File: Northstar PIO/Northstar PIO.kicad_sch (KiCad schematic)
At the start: 39 parts, among them J1 Conn_01x02, J1A1 Configuration Header, J2 Conn_01x02, J3 Conn_01x02, J4 Conn_01x02, J5 Conn_01x02, J6 Conn_01x02, J7 Conn_02x15_Odd_Even, P1 INPUT PORT, P2 OUTPUT PORT, U1B1 74LS74, U1C1 74LS74, U1D1 SN74LS164N, U2A1 74LS32, U2B1 74LS138, U2C1 74LS175, U2D1 74LS03, U2E1 74LS367, U3A1 74LS14, U3B1 74LS37, U3C1 74LS373, U3D1 74LS373

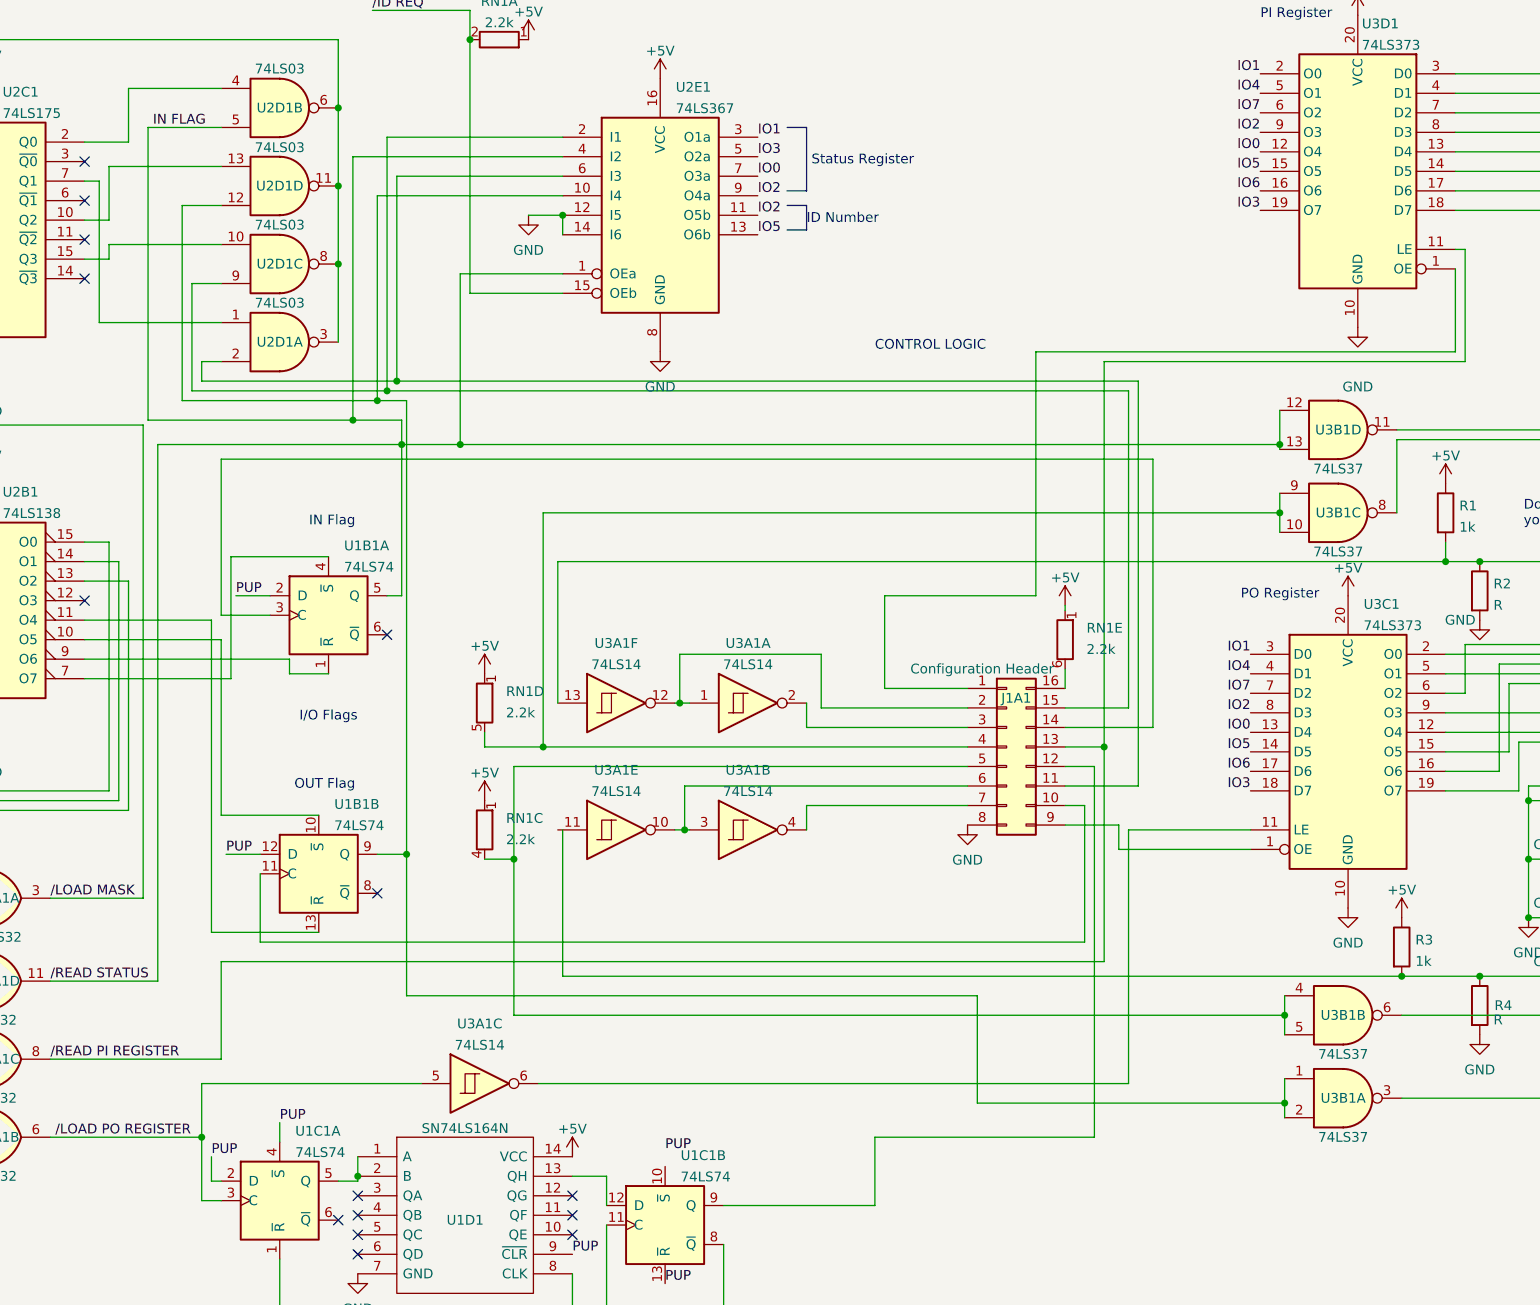
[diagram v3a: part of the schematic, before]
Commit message: fix pio problems discovered
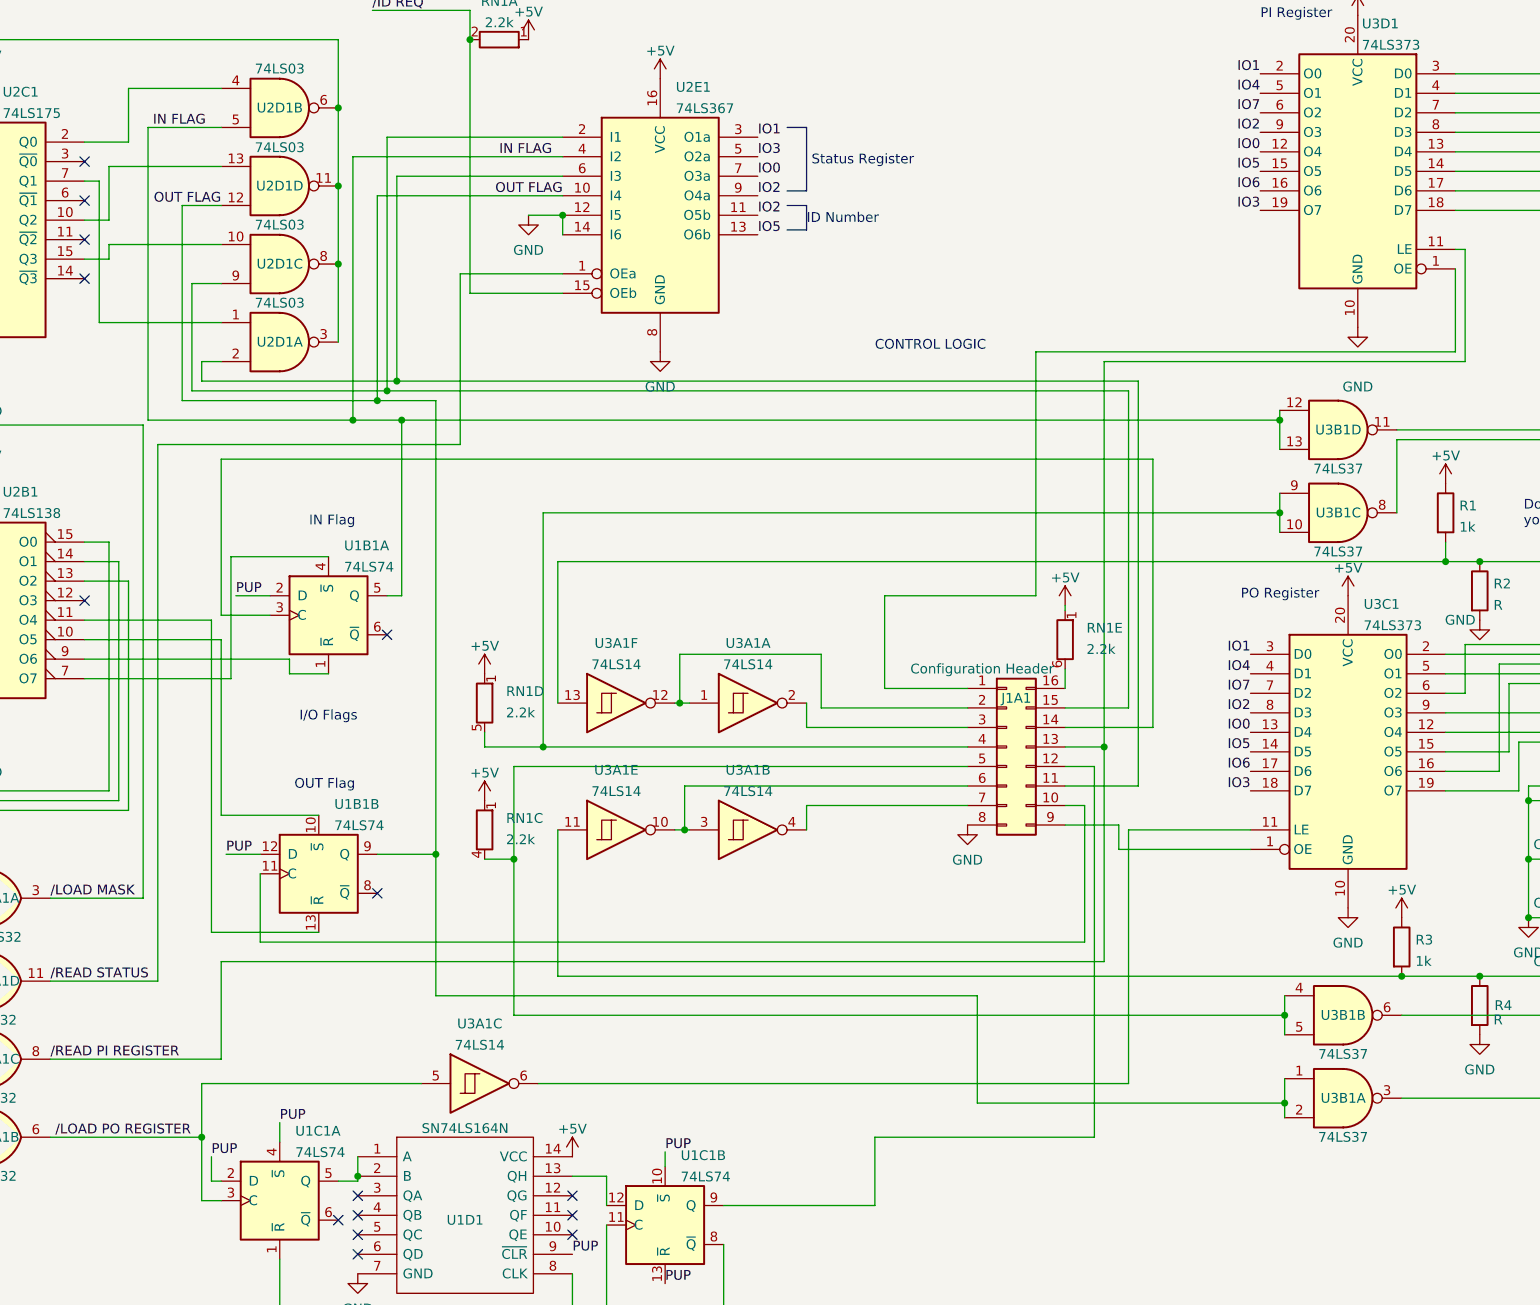
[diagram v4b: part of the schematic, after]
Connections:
- net IN FLAG: no longer U2A1.11, U2E1.1 (OEa)
- net PUP: now also U1C1.10 (~{S})
- net /OUT ACK: now also U3A1.11
- net OUT FLAG: now reaches U1B1.9 (Q), U2D1.12, U2E1.10 (I4), U3B1.1, U3B1.2
- new net /READ STATUS: U2A1.11, U2E1.1 (OEa)
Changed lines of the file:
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@@
   (junction (at 292.735 223.52) (diameter 0) (color 0 0 0 0)
   )
+  (junction (at 117.475 127) (diameter 0) (color 0 0 0 0)
+  )
   (junction (at 131.445 113.03) (diameter 0) (color 0 0 0 0)
   )
@@
   (junction (at 239.395 231.14) (diameter 0) (color 0 0 0 0)
   )
+  (junction (at 113.03 70.485) (diameter 0) (color 0 0 0 0)
+  )
   (junction (at 106.68 70.485) (diameter 0) (color 0 0 0 0)
   )
@@
   (junction (at 111.125 66.675) (diameter 0) (color 0 0 0 0)
   )
-  (junction (at 113.03 73.66) (diameter 0) (color 0 0 0 0)
-  )
-  (junction (at 120.65 73.66) (diameter 0) (color 0 0 0 0)
-  )
   (junction (at 227.33 82.55) (diameter 0) (color 0 0 0 0)
   )
@@
   (junction (at 253.365 142.875) (diameter 0) (color 0 0 0 0)
   )
-  (junction (at 113.665 127) (diameter 0) (color 0 0 0 0)
-  )
   (junction (at 239.395 223.52) (diameter 0) (color 0 0 0 0)
   )
@@
   (junction (at 149.225 107.315) (diameter 0) (color 0 0 0 0)
   )
+  (junction (at 227.33 70.485) (diameter 0) (color 0 0 0 0)
+  )
   (junction (at 186.055 223.52) (diameter 0) (color 0 0 0 0)
   )
@@
   )
   (junction (at 259.715 120.015) (diameter 0) (color 0 0 0 0)
-  )
-  (junction (at 227.33 73.66) (diameter 0) (color 0 0 0 0)
   )
   (junction (at 115.57 235.585) (diameter 0) (color 0 0 0 0)
@@
     (stroke (width 0) (type default) (color 0 0 0 0))
   )
-  (wire (pts (xy 109.855 67.945) (xy 113.665 67.945))
+  (wire (pts (xy 109.855 67.945) (xy 117.475 67.945))
     (stroke (width 0) (type default) (color 0 0 0 0))
   )
@@
     (stroke (width 0) (type default) (color 0 0 0 0))
   )
-  (wire (pts (xy 113.03 73.66) (xy 113.03 93.345))
-    (stroke (width 0) (type default) (color 0 0 0 0))
-  )
   (wire (pts (xy 104.775 40.005) (xy 104.775 29.845))
     (stroke (width 0) (type default) (color 0 0 0 0))
@@
     (stroke (width 0) (type default) (color 0 0 0 0))
   )
+  (wire (pts (xy 109.855 127) (xy 117.475 127))
+    (stroke (width 0) (type default) (color 0 0 0 0))
+  )
   (wire (pts (xy 43.18 71.12) (xy 43.18 54.61))
     (stroke (width 0) (type default) (color 0 0 0 0))
@@
     (stroke (width 0) (type default) (color 0 0 0 0))
   )
+  (wire (pts (xy 113.03 70.485) (xy 227.33 70.485))
+    (stroke (width 0) (type default) (color 0 0 0 0))
+  )
   (wire (pts (xy 270.51 120.015) (xy 266.065 120.015))
     (stroke (width 0) (type default) (color 0 0 0 0))
@@
     (stroke (width 0) (type default) (color 0 0 0 0))
   )
-  (wire (pts (xy 133.985 142.875) (xy 243.205 142.875))
+  (wire (pts (xy 133.35 142.875) (xy 243.205 142.875))
     (stroke (width 0) (type default) (color 0 0 0 0))
   )
@@
     (stroke (width 0) (type default) (color 0 0 0 0))
   )
+  (wire (pts (xy 227.33 70.485) (xy 227.33 74.295))
+    (stroke (width 0) (type default) (color 0 0 0 0))
+  )
   (wire (pts (xy 227.33 80.01) (xy 227.33 82.55))
     (stroke (width 0) (type default) (color 0 0 0 0))
@@
     (stroke (width 0) (type default) (color 0 0 0 0))
   )
+  (wire (pts (xy 147.32 165.735) (xy 147.32 167.64))
+    (stroke (width 0) (type default) (color 0 0 0 0))
+  )
   (wire (pts (xy 80.01 32.385) (xy 80.01 70.485))
     (stroke (width 0) (type default) (color 0 0 0 0))
@@
     (stroke (width 0) (type default) (color 0 0 0 0))
   )
-  (wire (pts (xy 113.665 127) (xy 113.665 145.415))
+  (wire (pts (xy 117.475 127) (xy 117.475 145.415))
     (stroke (width 0) (type default) (color 0 0 0 0))
   )
@@
     (stroke (width 0) (type default) (color 0 0 0 0))
   )
-  (wire (pts (xy 113.03 73.66) (xy 120.65 73.66))
-    (stroke (width 0) (type default) (color 0 0 0 0))
-  )
   (wire (pts (xy 267.335 47.625) (xy 267.335 55.88))
     (stroke (width 0) (type default) (color 0 0 0 0))
@@
     (stroke (width 0) (type default) (color 0 0 0 0))
   )
-  (wire (pts (xy 133.985 123.825) (xy 133.985 142.875))
+  (wire (pts (xy 133.35 123.825) (xy 133.35 142.875))
     (stroke (width 0) (type default) (color 0 0 0 0))
   )
@@
     (stroke (width 0) (type default) (color 0 0 0 0))
   )
-  (wire (pts (xy 113.665 67.945) (xy 113.665 127))
+  (wire (pts (xy 117.475 67.945) (xy 117.475 127))
     (stroke (width 0) (type default) (color 0 0 0 0))
   )
@@
     (stroke (width 0) (type default) (color 0 0 0 0))
   )
-  (wire (pts (xy 109.855 127) (xy 113.665 127))
-    (stroke (width 0) (type default) (color 0 0 0 0))
-  )
   (wire (pts (xy 127.635 127.635) (xy 127.635 147.955))
     (stroke (width 0) (type default) (color 0 0 0 0))
@@
     (stroke (width 0) (type default) (color 0 0 0 0))
   )
-  (wire (pts (xy 227.33 73.66) (xy 227.33 74.295))
-    (stroke (width 0) (type default) (color 0 0 0 0))
-  )
   (wire (pts (xy 94.615 138.43) (xy 201.93 138.43))
     (stroke (width 0) (type default) (color 0 0 0 0))
@@
     (stroke (width 0) (type default) (color 0 0 0 0))
   )
+  (wire (pts (xy 81.28 73.66) (xy 120.65 73.66))
+    (stroke (width 0) (type default) (color 0 0 0 0))
+  )
   (wire (pts (xy 199.39 115.57) (xy 203.2 115.57))
     (stroke (width 0) (type default) (color 0 0 0 0))
@@
     (stroke (width 0) (type default) (color 0 0 0 0))
   )
-  (wire (pts (xy 81.28 73.66) (xy 113.03 73.66))
-    (stroke (width 0) (type default) (color 0 0 0 0))
-  )
   (wire (pts (xy 299.085 109.855) (xy 299.085 118.11))
     (stroke (width 0) (type default) (color 0 0 0 0))
@@
     (stroke (width 0) (type default) (color 0 0 0 0))
   )
+  (wire (pts (xy 120.65 73.66) (xy 120.65 51.435))
+    (stroke (width 0) (type default) (color 0 0 0 0))
+  )
   (wire (pts (xy 19.685 20.955) (xy 104.775 20.955))
     (stroke (width 0) (type default) (color 0 0 0 0))
@@
     (stroke (width 0) (type default) (color 0 0 0 0))
   )
-  (wire (pts (xy 113.665 145.415) (xy 187.96 145.415))
+  (wire (pts (xy 117.475 145.415) (xy 187.96 145.415))
     (stroke (width 0) (type default) (color 0 0 0 0))
   )
@@
     (stroke (width 0) (type default) (color 0 0 0 0))
   )
-  (wire (pts (xy 120.65 51.435) (xy 120.65 73.66))
-    (stroke (width 0) (type default) (color 0 0 0 0))
-  )
   (wire (pts (xy 295.91 33.655) (xy 304.8 33.655))
     (stroke (width 0) (type default) (color 0 0 0 0))
@@
     (stroke (width 0) (type default) (color 0 0 0 0))
   )
-  (wire (pts (xy 227.33 69.215) (xy 227.33 73.66))
+  (wire (pts (xy 227.33 69.215) (xy 227.33 70.485))
     (stroke (width 0) (type default) (color 0 0 0 0))
   )
@@
     (stroke (width 0) (type default) (color 0 0 0 0))
   )
-  (wire (pts (xy 120.65 73.66) (xy 227.33 73.66))
-    (stroke (width 0) (type default) (color 0 0 0 0))
-  )
   (wire (pts (xy 71.755 34.29) (xy 77.47 34.29))
     (stroke (width 0) (type default) (color 0 0 0 0))
@@
     (stroke (width 0) (type default) (color 0 0 0 0))
   )
-  (wire (pts (xy 113.03 73.66) (xy 113.03 70.485))
+  (wire (pts (xy 113.03 70.485) (xy 113.03 93.345))
     (stroke (width 0) (type default) (color 0 0 0 0))
   )
@@
     (effects (font (size 1.27 1.27)) (justify left bottom))
   )
+  (label "OUT FLAG" (at 133.985 41.275 180)
+    (effects (font (size 1.27 1.27)) (justify right bottom))
+  )
   (label "IO1" (at 224.79 25.4 180)
     (effects (font (size 1.27 1.27)) (justify right bottom))
@@
     (effects (font (size 1.27 1.27)) (justify left bottom))
   )
+  (label "IN FLAG" (at 125.73 36.195 0)
+    (effects (font (size 1.27 1.27)) (justify left bottom))
+  )
   (label "{slash}BIO RES" (at 49.53 222.885 0)
     (effects (font (size 1.27 1.27)) (justify left bottom))
@@
     (effects (font (size 1.27 1.27)) (justify left bottom))
   )
+  (label "OUT FLAG" (at 89.535 42.545 180)
+    (effects (font (size 1.27 1.27)) (justify right bottom))
+  )
   (label "{slash}BRD" (at 36.83 217.805 180)
